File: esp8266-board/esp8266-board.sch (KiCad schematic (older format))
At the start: 1 part

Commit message: WIP
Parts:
- added C1: 330uF, Capacitors_THT:CP_Axial_L18.0mm_D10.0mm_P25.00mm_Horizontal, symbol CP
- added C2: 0.1uF, Capacitors_SMD:C_1206_HandSoldering, symbol C
- added C3: 1uF, Capacitors_SMD:C_1206_HandSoldering, symbol C
- added J1: StepDown-3A, Pin_Headers:Pin_Header_Straight_1x04_Pitch2.54mm, symbol StepDown-3A
- added J2: Barrel_Jack, libraries:5.5mm_Barrel_Jack, symbol Barrel_Jack
- added J3: USB, Connectors:USB_Micro-B, symbol USB_OTG
- added J4: LED, Pin_Headers:Pin_Header_Straight_1x04_Pitch2.54mm, symbol Conn_01x04
- added J5: PGM, Pin_Headers:Pin_Header_Straight_1x05_Pitch2.54mm, symbol Conn_01x05
- added JP1: WAKE, libraries:SolderJumper, symbol Jumper_NO_Small
- added R1, R2, R3, R4, R5: 10k, Resistors_SMD:R_1206_HandSoldering, symbol R
- U1: renamed from U?; footprint (none) -> ESP8266:ESP-12E
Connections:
- net ~RST: now reaches U1.1 (REST)
- net ~RST: now also J5.3 (Pin_3), JP1.1, R1.1
- net at U1.10 (GPIO15): now also R5.2
- net at U1.11 (GPIO2): now also R4.2
- net ~FLASH: now reaches U1.12 (GPIO0)
- net ~FLASH: now also J5.2 (Pin_2), R3.2
- net GPIO4: now reaches U1.13 (GPIO4)
- net GPIO4: now also J4.3 (Pin_3)
- net GPIO5: now reaches U1.14 (GPIO5)
- net GPIO5: now also J4.4 (Pin_4)
- net RX: now reaches U1.15 (RXD)
- net RX: now also J5.5 (Pin_5)
- net TX: now reaches U1.16 (TXD)
- net TX: now also J5.4 (Pin_4)
- net ADC: now reaches U1.2 (ADC)
- net at U1.3 (CH_PD): now also R2.1
- net GPIO16: now reaches U1.4 (GPIO16)
- net GPIO16: now also JP1.2
- net GPIO14: now reaches U1.5 (GPIO14)
- net GPIO12: now reaches U1.6 (GPIO12)
- net GPIO13: now reaches U1.7 (GPIO13)
- net +3V3: now reaches U1.8 (VCC)
- net +3V3: now also C1.1, C2.2, C3.2, J1.4 (VO+), R1.2, R2.2, R3.1, R4.1
- net GND: now reaches U1.9 (GND)
- net GND: now also C1.2, C2.1, C3.1, J1.3 (GND), J2.2, J3.5 (GND), J4.2 (Pin_2), J5.1 (Pin_1), R5.1
- new net +5V: J1.2 (IN+), J2.1, J3.1 (VBUS), J4.1 (Pin_1)
- no-connect marks 0 -> 16

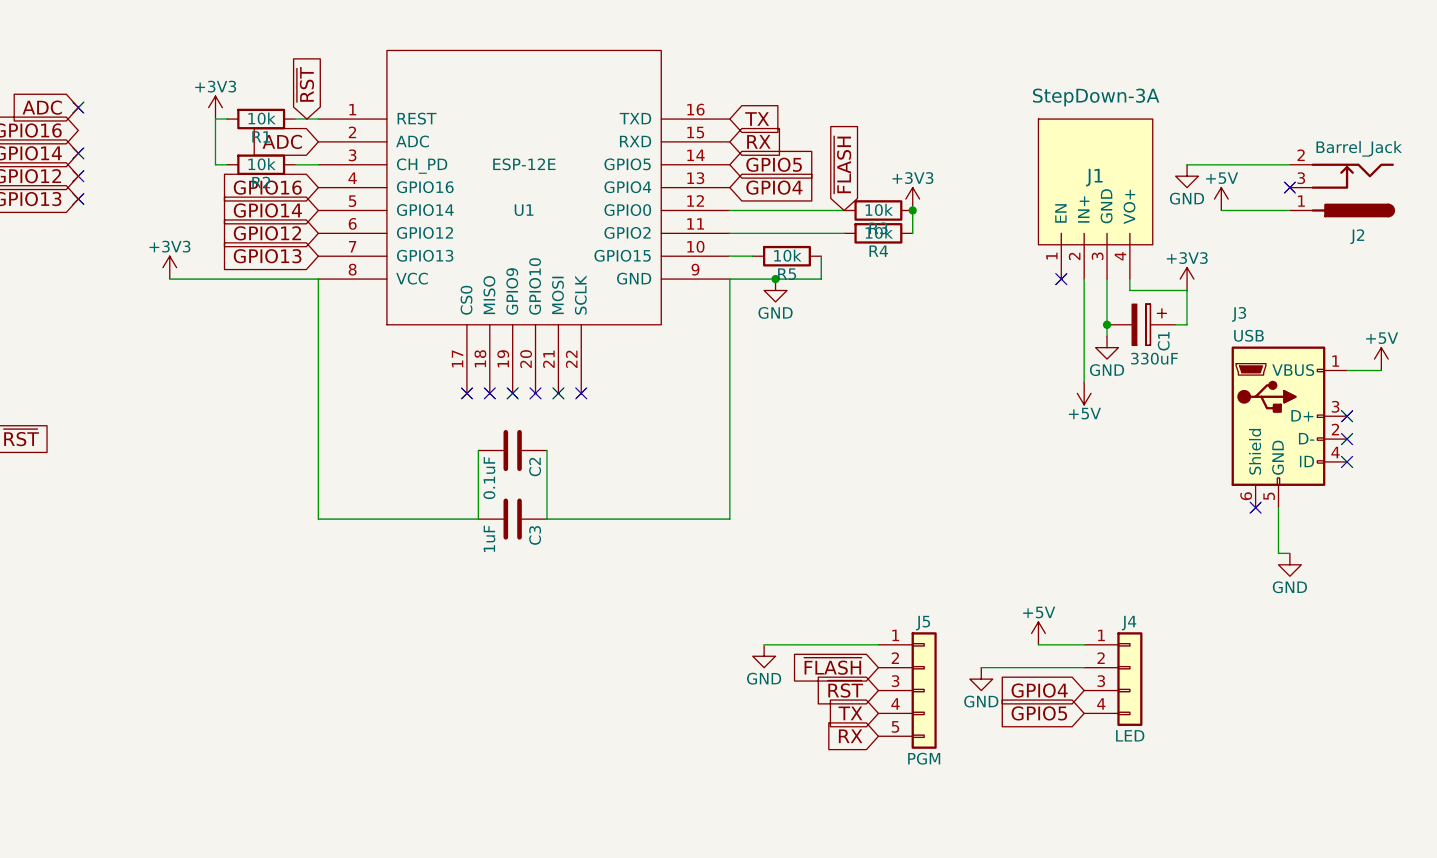
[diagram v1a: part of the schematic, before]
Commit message: Reogranizing and making use of new footprints
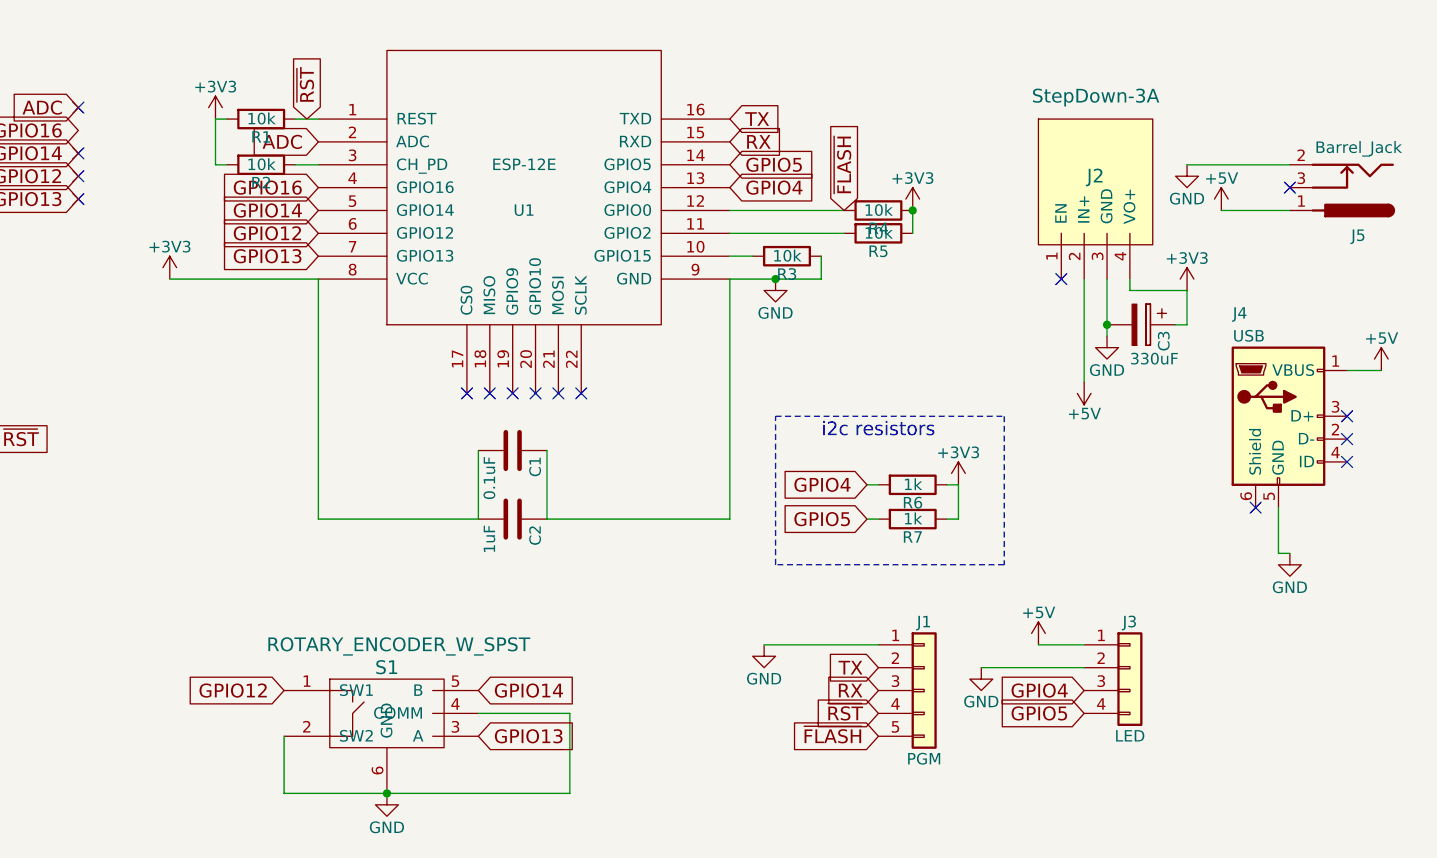
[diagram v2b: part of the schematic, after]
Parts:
- added R6, R7: 1k, Resistors_SMD:R_1206_HandSoldering, symbol R
- added S1: ROTARY_ENCODER_W_SPST, Switches:Rotary_Encoder_Or_Switch, symbol ROTARY_ENCODER_W_SPST
- J2: renamed from J1; footprint Pin_Headers:Pin_Header_Straight_1x04_Pitch2.54mm -> Voltage Regulators:SwitchingRegulator_Selectable
- J5: renamed from J2; footprint libraries:5.5mm_Barrel_Jack -> Power:5.5mm_Barrel_Jack
- JP1: footprint libraries:SolderJumper -> Features:SolderJumper
- renumbered C2 to C1, C3 to C2, C1 to C3, J5 to J1, J4 to J3, J3 to J4, R5 to R3, R3 to R4, R4 to R5
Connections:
- net +3V3: now also R6.1, R7.1
- net GND: now also S1.2 (SW2), S1.4 (COMM), S1.6 (GND)
- net GPIO12: now also S1.1 (SW1)
- net GPIO13: now also S1.3 (A)
- net GPIO14: now also S1.5 (B)
- net GPIO4: now also R6.2
- net GPIO5: now also R7.2
- net RX: now also J1.3 (Pin_3); no longer J1.5 (Pin_5)
- net TX: now also J1.2 (Pin_2); no longer J1.4 (Pin_4)
- net ~FLASH: now also J1.5 (Pin_5); no longer J1.2 (Pin_2)
- net ~RST: now also J1.4 (Pin_4); no longer J1.3 (Pin_3)
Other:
- note added: "i2c resistors"
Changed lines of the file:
@@
 LIBS:contrib
 LIBS:valves
-LIBS:ESP8266
+LIBS:switches_inputs
 LIBS:voltage-regulators
 LIBS:esp8266-board-cache
@@
 $EndComp
 $Comp
-L StepDown-3A J1
+L StepDown-3A J2
 U 1 1 5A00ECE4
 P 7300 2650
-F 0 "J1" H 7300 2650 60  0000 C CNN
+F 0 "J2" H 7300 2650 60  0000 C CNN
 F 1 "StepDown-3A" H 7300 3000 60  0000 C CNN
-F 2 "Pin_Headers:Pin_Header_Straight_1x04_Pitch2.54mm" H 7300 2650 60  0001 C CNN
+F 2 "Voltage Regulators:SwitchingRegulator_Selectable" H 7300 2650 60  0001 C CNN
 F 3 "" H 7300 2650 60  0001 C CNN
 	1    7300 2650
@@
 $EndComp
 $Comp
-L USB_OTG J3
+L USB_OTG J4
 U 1 1 5A00ED3B
 P 8100 3700
-F 0 "J3" H 7900 4150 50  0000 L CNN
+F 0 "J4" H 7900 4150 50  0000 L CNN
 F 1 "USB" H 7900 4050 50  0000 L CNN
 F 2 "Connectors:USB_Micro-B" H 8250 3650 50  0001 C CNN
@@
 $EndComp
 $Comp
-L Barrel_Jack J2
+L Barrel_Jack J5
 U 1 1 5A00EF7E
 P 8450 2700
-F 0 "J2" H 8450 2910 50  0000 C CNN
+F 0 "J5" H 8450 2910 50  0000 C CNN
 F 1 "Barrel_Jack" H 8450 2525 50  0000 C CNN
-F 2 "libraries:5.5mm_Barrel_Jack" H 8500 2660 50  0001 C CNN
+F 2 "Power:5.5mm_Barrel_Jack" H 8500 2660 50  0001 C CNN
 F 3 "" H 8500 2660 50  0001 C CNN
 	1    8450 2700
@@
 	3500 2400 3450 2400
 $Comp
-L CP C1
+L CP C3
 U 1 1 5A00F26E
 P 7500 3300
-F 0 "C1" H 7525 3400 50  0000 L CNN
+F 0 "C3" H 7525 3400 50  0000 L CNN
 F 1 "330uF" V 7650 3250 50  0000 L CNN
 F 2 "Capacitors_THT:CP_Axial_L18.0mm_D10.0mm_P25.00mm_Horizontal" H 7538 3150 50  0001 C CNN
@@
 	7450 3150 7450 3100
 $Comp
-L C C3
+L C C2
 U 1 1 5A010134
 P 4750 4150
-F 0 "C3" H 4775 4250 50  0000 L CNN
+F 0 "C2" H 4775 4250 50  0000 L CNN
 F 1 "1uF" H 4775 4050 50  0000 L CNN
 F 2 "Capacitors_SMD:C_1206_HandSoldering" H 4788 4000 50  0001 C CNN
@@
 $EndComp
 $Comp
-L R R3
+L R R4
 U 1 1 5A010263
 P 6350 2800
-F 0 "R3" V 6430 2800 50  0000 C CNN
+F 0 "R4" V 6430 2800 50  0000 C CNN
 F 1 "10k" V 6350 2800 50  0000 C CNN
 F 2 "Resistors_SMD:R_1206_HandSoldering" V 6280 2800 50  0001 C CNN
@@
 	5700 2800 6200 2800
 $Comp
-L R R4
+L R R5
 U 1 1 5A0108BC
 P 6350 2900
-F 0 "R4" V 6430 2900 50  0000 C CNN
+F 0 "R5" V 6430 2900 50  0000 C CNN
 F 1 "10k" V 6350 2900 50  0000 C CNN
 F 2 "Resistors_SMD:R_1206_HandSoldering" V 6280 2900 50  0001 C CNN
@@
 	6200 2900 5700 2900
 $Comp
-L R R5
+L R R3
 U 1 1 5A0109BD
 P 5950 3000
-F 0 "R5" V 6030 3000 50  0000 C CNN
+F 0 "R3" V 6030 3000 50  0000 C CNN
 F 1 "10k" V 5950 3000 50  0000 C CNN
 F 2 "Resistors_SMD:R_1206_HandSoldering" V 5880 3000 50  0001 C CNN
@@
 Wire Wire Line
 	3450 2600 3450 2400
-Text GLabel 6350 4800 0    60   Input ~ 0
+Text GLabel 6350 5100 0    60   Input ~ 0
 ~FLASH
-Text GLabel 6350 4900 0    60   Input ~ 0
+Text GLabel 6350 5000 0    60   Input ~ 0
 ~RST
 Text GLabel 5700 2400 2    60   Input ~ 0
@@
 GPIO13
 $Comp
-L Conn_01x05 J5
+L Conn_01x05 J1
 U 1 1 5A0111F1
 P 6550 4900
-F 0 "J5" H 6550 5200 50  0000 C CNN
+F 0 "J1" H 6550 5200 50  0000 C CNN
 F 1 "PGM" H 6550 4600 50  0000 C CNN
 F 2 "Pin_Headers:Pin_Header_Straight_1x05_Pitch2.54mm" H 6550 4900 50  0001 C CNN
@@
 Wire Wire Line
 	5850 4700 6350 4700
-Text GLabel 6350 5000 0    60   Input ~ 0
+Text GLabel 6350 4800 0    60   Input ~ 0
 TX
-Text GLabel 6350 5100 0    60   Input ~ 0
+Text GLabel 6350 4900 0    60   Input ~ 0
 RX
 $Comp
-L Conn_01x04 J4
+L Conn_01x04 J3
 U 1 1 5A011626
 P 7450 4800
-F 0 "J4" H 7450 5000 50  0000 C CNN
+F 0 "J3" H 7450 5000 50  0000 C CNN
 F 1 "LED" H 7450 4500 50  0000 C CNN
 F 2 "Pin_Headers:Pin_Header_Straight_1x04_Pitch2.54mm" H 7450 4800 50  0001 C CNN
@@
 F 0 "JP1" H 2350 3880 50  0000 C CNN
 F 1 "WAKE" H 2360 3740 50  0000 C CNN
-F 2 "libraries:SolderJumper" H 2350 3800 50  0001 C CNN
+F 2 "Features:SolderJumper" H 2350 3800 50  0001 C CNN
 F 3 "" H 2350 3800 50  0001 C CNN
 	1    2350 3800
@@
 NoConn ~ 7150 3100
 $Comp
-L C C2
+L C C1
 U 1 1 5A012B7F
 P 4750 3850
-F 0 "C2" H 4775 3950 50  0000 L CNN
+F 0 "C1" H 4775 3950 50  0000 L CNN
 F 1 "0.1uF" H 4775 3750 50  0000 L CNN
 F 2 "Capacitors_SMD:C_1206_HandSoldering" H 4788 3700 50  0001 C CNN
@@
 Wire Wire Line
 	4600 3850 4600 4150
+$Comp
+L ROTARY_ENCODER_W_SPST S1
+U 1 1 5A074E2B
+P 4200 5000
+F 0 "S1" H 4200 5200 60  0000 C CNN
+F 1 "ROTARY_ENCODER_W_SPST" H 4250 5300 60  0000 C CNN
+F 2 "Switches:Rotary_Encoder_Or_Switch" H 4050 4850 60  0001 C CNN
+F 3 "" H 4050 4850 60  0001 C CNN
+	1    4200 5000
+	1    0    0    -1
+$EndComp
+$Comp
+L GND #PWR015
+U 1 1 5A074EAE
+P 4200 5350
+F 0 "#PWR015" H 4200 5100 50  0001 C CNN
+F 1 "GND" H 4200 5200 50  0000 C CNN
+F 2 "" H 4200 5350 50  0001 C CNN
+F 3 "" H 4200 5350 50  0001 C CNN
+	1    4200 5350
+	1    0    0    -1
+$EndComp
+Wire Wire Line
+	3750 5350 5000 5350
+Wire Wire Line
+	3750 5350 3750 5100
+Wire Wire Line
+	5000 5350 5000 5000
+Wire Wire Line
+	5000 5000 4600 5000
+Connection ~ 4200 5350
+Text GLabel 3750 4900 0    60   Input ~ 0
+GPIO12
+Text GLabel 4600 5100 2    60   Input ~ 0
+GPIO13
+Text GLabel 4600 4900 2    60   Input ~ 0
+GPIO14
+$Comp
+L +3V3 #PWR016
+U 1 1 5A0763B7
+P 6700 4000
+F 0 "#PWR016" H 6700 3850 50  0001 C CNN
+F 1 "+3V3" H 6700 4140 50  0000 C CNN
+F 2 "" H 6700 4000 50  0001 C CNN
+F 3 "" H 6700 4000 50  0001 C CNN
+	1    6700 4000
+	1    0    0    -1
+$EndComp
+Text GLabel 6300 4000 0    60   Input ~ 0
+GPIO4
+Text GLabel 6300 4150 0    60   Input ~ 0
+GPIO5
+$Comp
+L R R6
+U 1 1 5A0768D9
+P 6500 4000
+F 0 "R6" V 6580 4000 50  0000 C CNN
+F 1 "1k" V 6500 4000 50  0000 C CNN
+F 2 "Resistors_SMD:R_1206_HandSoldering" V 6430 4000 50  0001 C CNN
+F 3 "" H 6500 4000 50  0001 C CNN
+	1    6500 4000
+	0    1    1    0
+$EndComp
+$Comp
+L R R7
+U 1 1 5A0768E1
+P 6500 4150
+F 0 "R7" V 6580 4150 50  0000 C CNN
+F 1 "1k" V 6500 4150 50  0000 C CNN
+F 2 "Resistors_SMD:R_1206_HandSoldering" V 6430 4150 50  0001 C CNN
+F 3 "" H 6500 4150 50  0001 C CNN
+	1    6500 4150
+	0    1    1    0
+$EndComp
+Wire Wire Line
+	6650 4150 6700 4150
+Wire Wire Line
+	6700 4150 6700 4000
+Wire Wire Line
+	6700 4000 6650 4000
+Wire Wire Line
+	6350 4000 6300 4000
+Wire Wire Line
+	6300 4150 6350 4150
+Wire Notes Line
+	5900 3700 6900 3700
+Wire Notes Line
+	6900 3700 6900 4350
+Wire Notes Line
+	6900 4350 5900 4350
+Wire Notes Line
+	5900 4350 5900 3700
+Text Notes 6100 3800 0    60   ~ 0
+i2c resistors
 $EndSCHEMATC

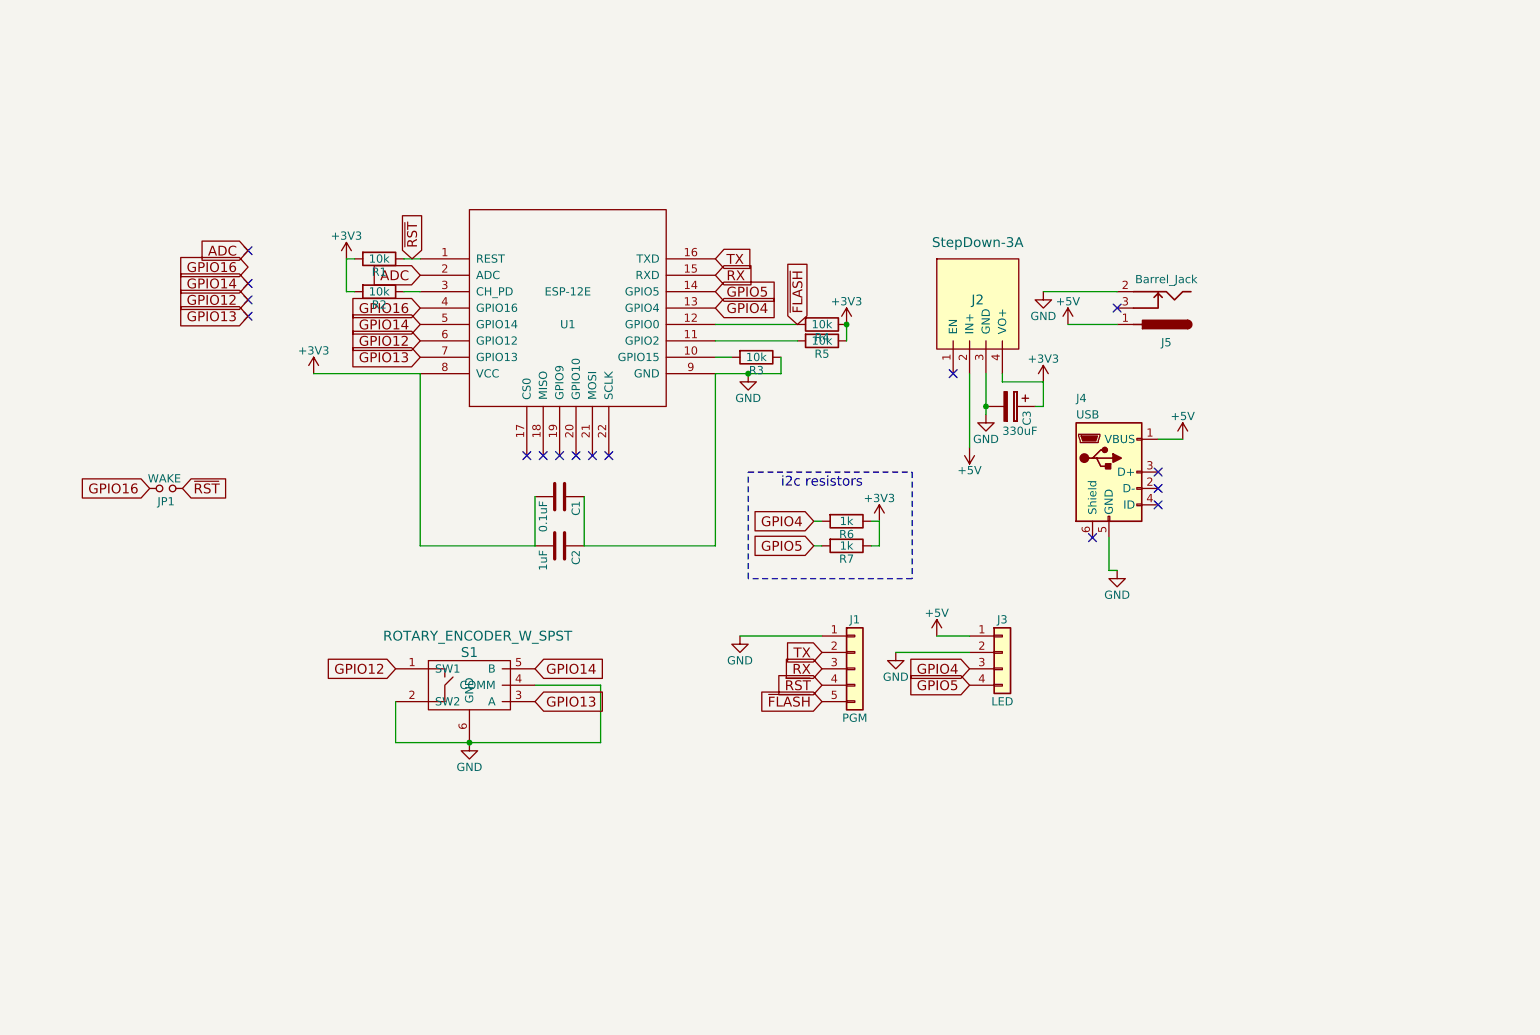
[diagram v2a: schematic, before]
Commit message: New voltage regulation structure in process
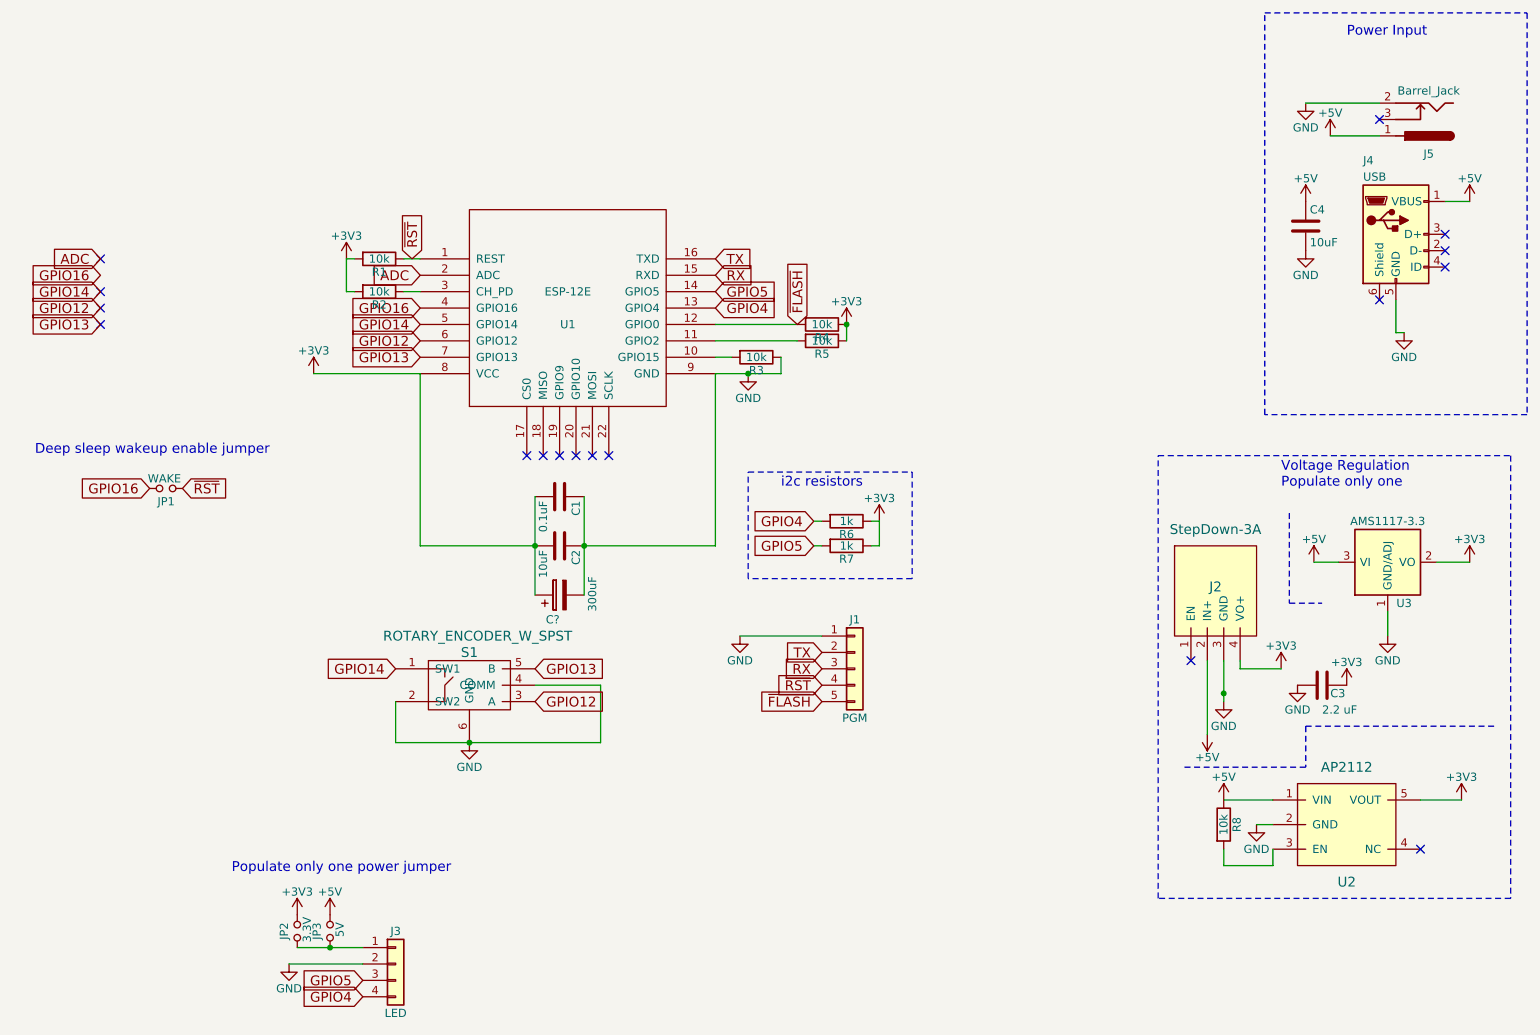
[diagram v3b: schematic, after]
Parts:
- removed C3: 330uF, Capacitors_THT:CP_Axial_L18.0mm_D10.0mm_P25.00mm_Horizontal, symbol CP
- added C3: 2.2 uF, Capacitors_SMD:C_1206_HandSoldering, symbol C
- added C4: 10uF, Capacitors_SMD:C_1206_HandSoldering, symbol C
- added C?: 300uF, symbol CP
- added JP2: 3.3V, Features:SolderJumper, symbol Jumper_NO_Small
- added JP3: 5V, Features:SolderJumper, symbol Jumper_NO_Small
- added R8: 10k, Resistors_SMD:R_1206_HandSoldering, symbol R
- added U2: AP2112, TO_SOT_Packages_SMD:SOT-23-5, symbol AP2112
- added U3: AMS1117-3.3, TO_SOT_Packages_SMD:SOT-223, symbol AMS1117-3.3
- C2: value 1uF -> 10uF
- R6, R7: footprint Resistors_SMD:R_1206_HandSoldering -> Resistors_SMD:R_0805_HandSoldering
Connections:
- net +3V3: now also C3.1, C?.1, JP2.2, U2.5 (VOUT), U3.2 (VO), U3.4 (VO)
- net +5V: now also C4.1, JP3.2, R8.1, U2.1 (VIN), U3.3 (VI); no longer J3.1 (Pin_1)
- net GND: now also C3.2, C4.2, C?.2, U2.2 (GND), U3.1 (GND/ADJ)
- net GPIO12: now also S1.3 (A); no longer S1.1 (SW1)
- net GPIO13: now also S1.5 (B); no longer S1.3 (A)
- net GPIO14: now also S1.1 (SW1); no longer S1.5 (B)
- net GPIO4: now also J3.4 (Pin_4); no longer J3.3 (Pin_3)
- net GPIO5: now also J3.3 (Pin_3); no longer J3.4 (Pin_4)
- new net: J3.1 (Pin_1), JP2.1, JP3.1
- new net: R8.2, U2.3 (EN)
- no-connect marks 16 -> 17
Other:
- note added: "Deep sleep wakeup enable jumper"
- note added: "Populate only one power jumper"
- note added: "Power Input"
- note added: "Voltage Regulation\nPopulate only one"
- moved on the sheet: J2, J3, J4, J5
